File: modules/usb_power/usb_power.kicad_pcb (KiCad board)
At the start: 2 copper layers, 30.5 x 68.6 mm, 11 parts, among them J1 USB_C_Receptacle_PowerOnly_6P

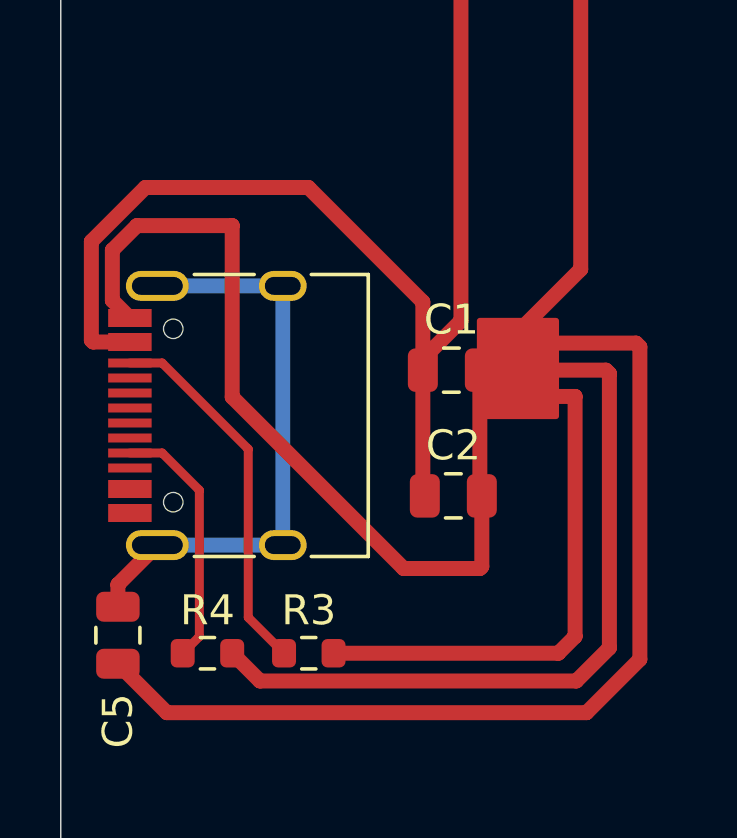
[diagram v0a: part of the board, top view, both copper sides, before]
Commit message: Changed the orientation of the USB C port
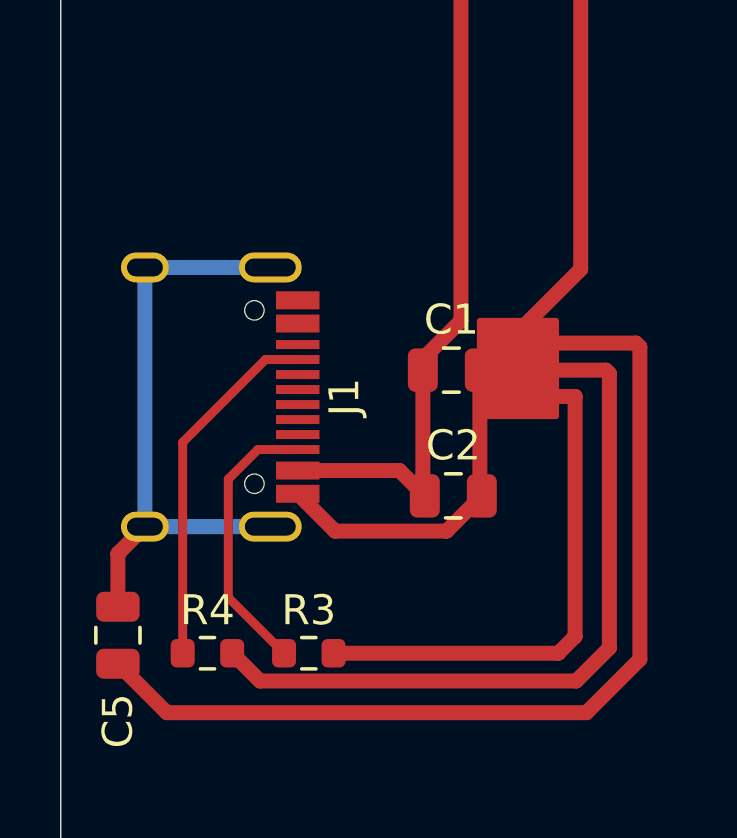
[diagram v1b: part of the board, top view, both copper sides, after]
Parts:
- J1: footprint Connector_USB:USB_C_Receptacle_HRO_TYPE-C-31-M-12 -> BreadModular_TypeC:HRO-TYPE-C-31-M-12
- moved J1 6.18 mm to (47.2, 74.9), turned to -90 degrees
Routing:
- net GND: track 197.5 -> 179.0 mm
- net Net-(C1-Pad1): track 39.0 -> 23.3 mm
- net Net-(J1-CC1): track 8.49 -> 12.0 mm
- net Net-(J1-CC2): track 12.4 -> 9.30 mm

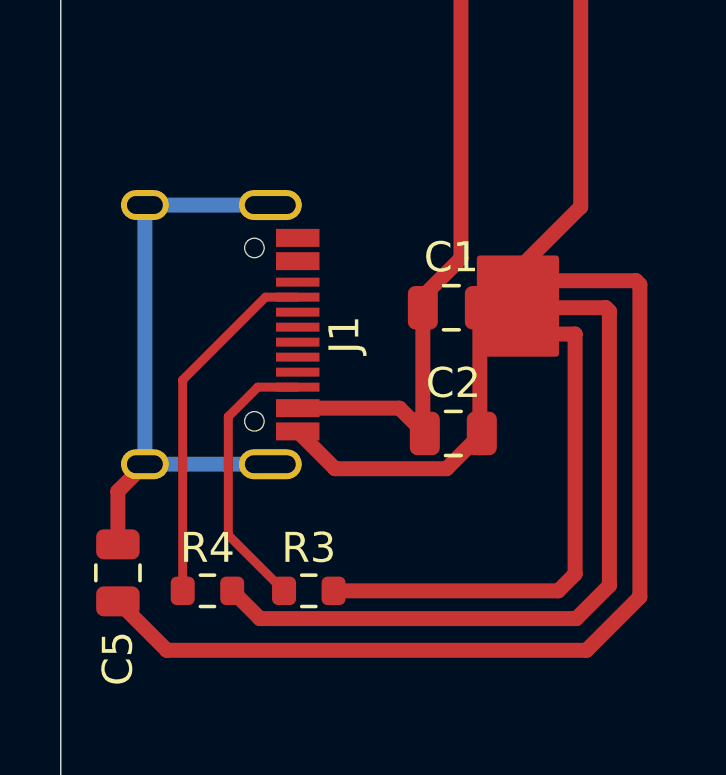
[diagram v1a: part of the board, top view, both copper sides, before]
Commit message: Change usb_power for the TypeC footprint update.
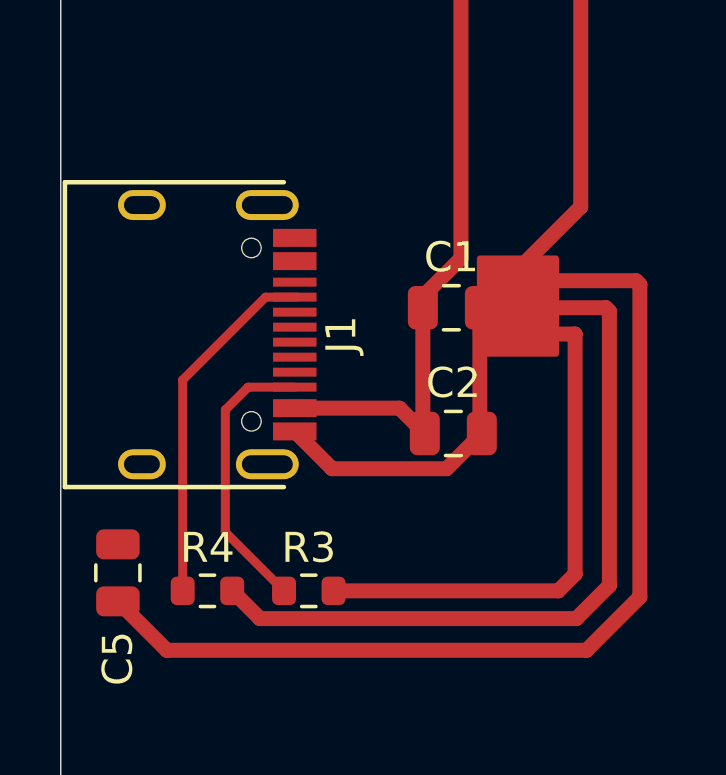
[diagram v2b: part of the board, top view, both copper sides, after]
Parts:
- moved J1 0.10 mm to (47.1, 74.9)
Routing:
- net Net-(J1-SHIELD): track 20.0 -> 0.00 mm

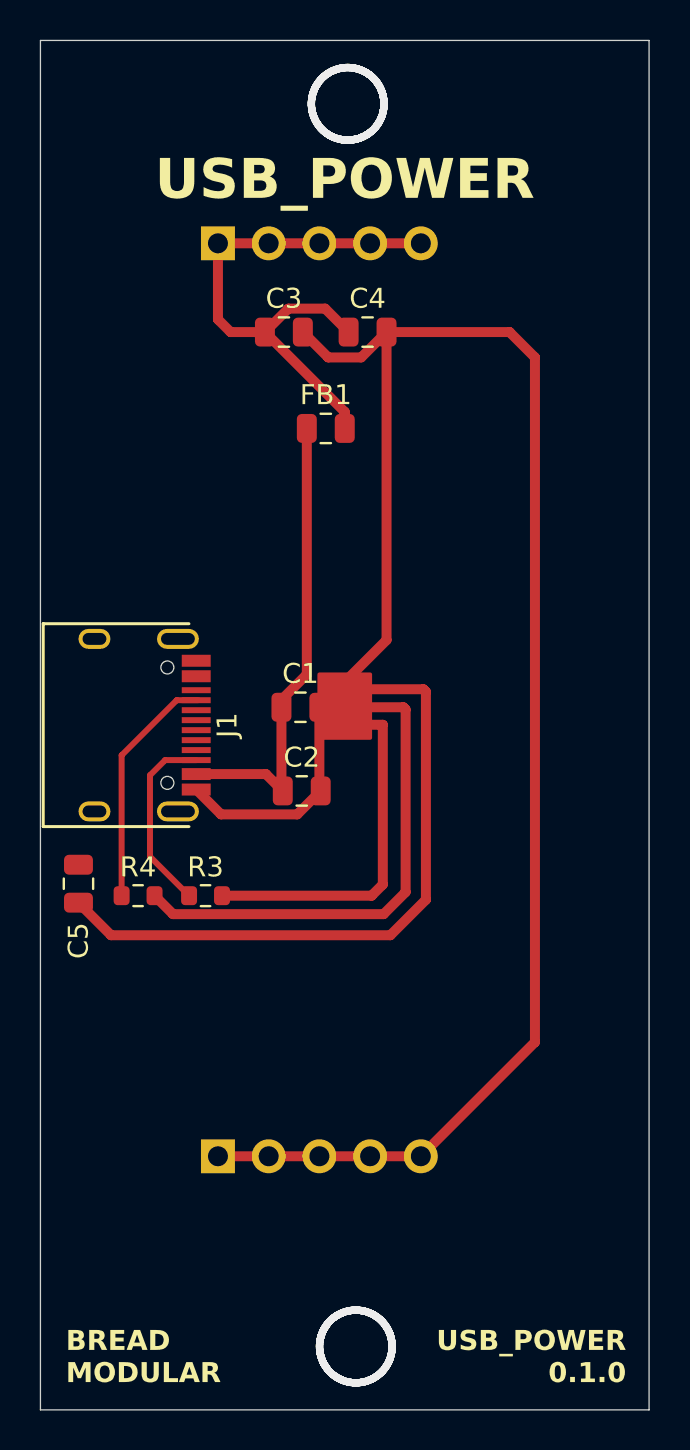
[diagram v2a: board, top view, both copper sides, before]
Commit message: Update usb_power to regulate as 3.3V
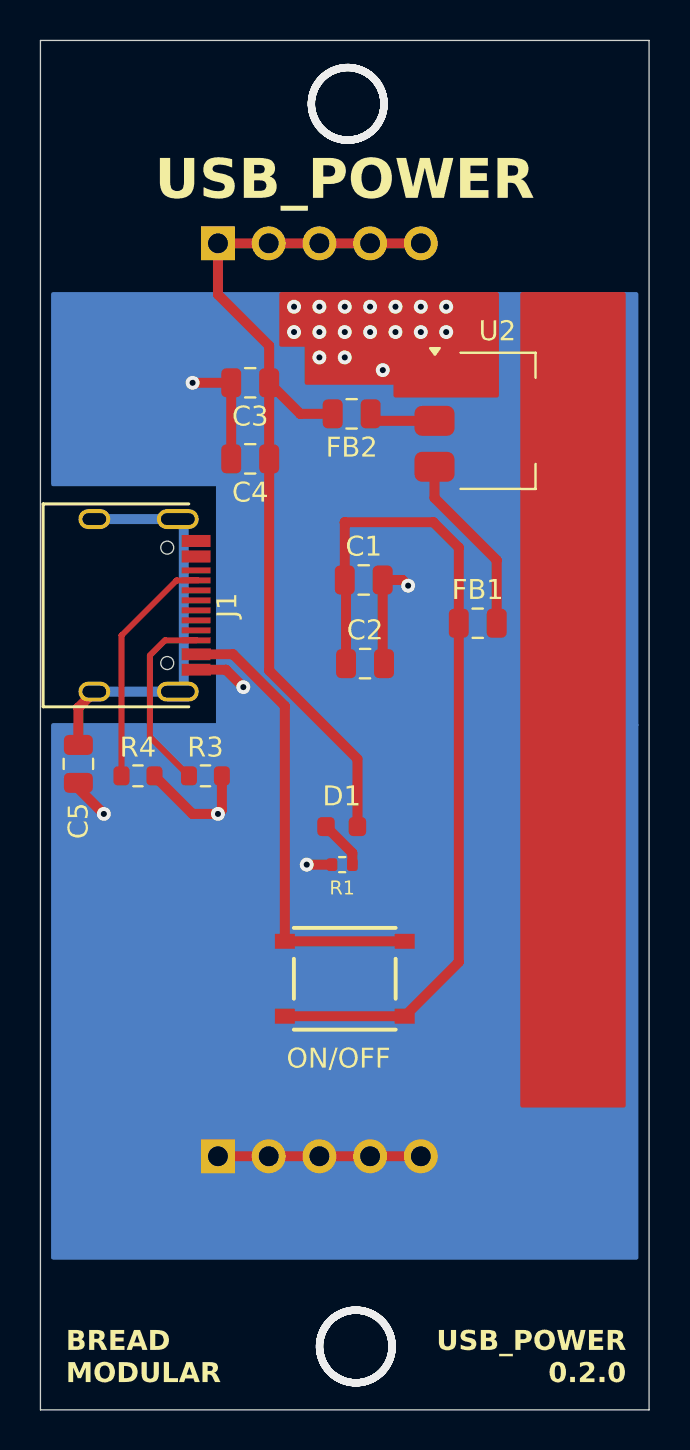
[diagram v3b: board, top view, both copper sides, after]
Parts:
- added D1: LED, LED_SMD:LED_0603_1608Metric, F.Cu at (62.1, 80.0)
- added FB2: GZ2012E800TF, Capacitor_SMD:C_0805_2012Metric, F.Cu at (62.6, 59.3)
- added R1: 1k, Resistor_SMD:R_0402_1005Metric, F.Cu at (62.1, 81.9)
- added SW1: SW_SPST, BreadModular_MISC:SPST_TS-1187A-B-A-B, F.Cu at (62.2, 87.6)
- added U2: AMS1117-3.3, Package_TO_SOT_SMD:SOT-223, F.Cu at (69.9, 59.7)
- moved FB1 12.4 mm to (68.9, 69.8)
- moved C4 8.65 mm to (57.5, 61.6), turned to 180 degrees
- moved C1 7.12 mm to (63.2, 67.7)
- moved C2 7.12 mm to (63.2, 71.9)
- moved C5 6.00 mm to (48.9, 76.9)
- moved J1 6.00 mm to (47.1, 68.9)
- moved R3 6.00 mm to (55.3, 77.5)
- moved R4 6.00 mm to (51.9, 77.5)
- moved C3 3.05 mm to (57.5, 57.8), turned to 180 degrees
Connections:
- 5V1 pad 1: +5V -> +3.3V
- 5V1 pad 2: +5V -> +3.3V
- 5V1 pad 3: +5V -> +3.3V
- 5V1 pad 4: +5V -> +3.3V
- 5V1 pad 5: +5V -> +3.3V
- C1 pad 1: Net-(C1-Pad1) -> Net-(SW1-B)
- C2 pad 1: Net-(C1-Pad1) -> Net-(SW1-B)
- C3 pad 1: +5V -> +3.3V
- C4 pad 1: +5V -> +3.3V
- FB1 pad 1: Net-(C1-Pad1) -> Net-(SW1-B)
- FB1 pad 2: +5V -> Net-(U2-VI)
- J1 pad A9: Net-(C1-Pad1) -> Net-(SW1-A)
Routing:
- net GND: track 179.1 -> 36.2 mm, vias 0 -> 23
- net +3.3V: track 0.00 -> 46.1 mm
- net Net-(SW1-B): track 0.00 -> 43.9 mm
- net +5V: track 28.2 -> 0.00 mm
- net Net-(SW1-A): track 0.00 -> 23.3 mm
- net Net-(C1-Pad1): track 23.3 -> 0.00 mm
- net Net-(J1-SHIELD): track 0.00 -> 20.2 mm
- net Net-(U2-VI): track 0.00 -> 9.13 mm
- net Net-(U2-VO): track 0.00 -> 3.34 mm
- net Net-(D1-K): track 0.00 -> 2.45 mm
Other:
- board text added: "ON/OFF"
- board text added: "USB_POWER 0.2.0"
- board text removed: "USB_POWER 0.1.0"

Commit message: Removed the usb_power tactile switch
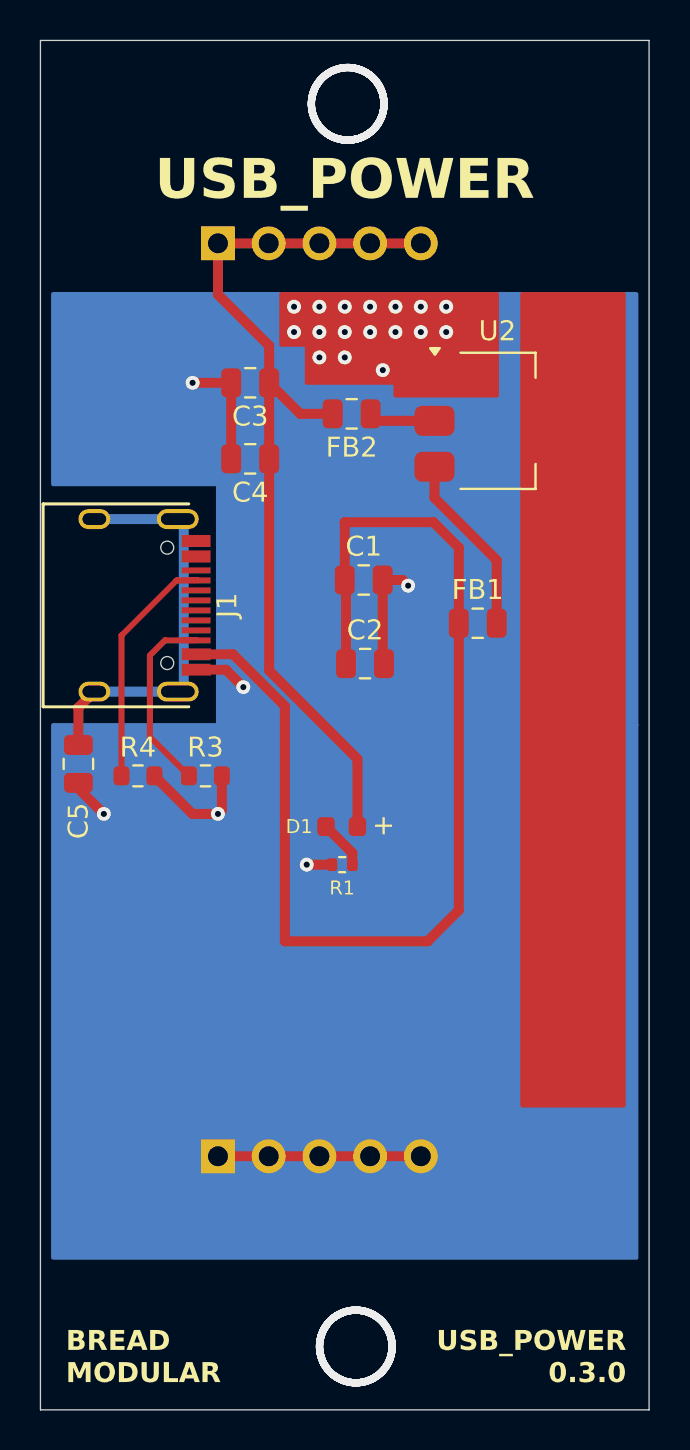
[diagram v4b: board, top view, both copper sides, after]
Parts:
- removed SW1: SW_SPST, BreadModular_MISC:SPST_TS-1187A-B-A-B
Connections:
- C1 pad 1: Net-(SW1-B) -> Net-(C1-Pad1)
- C2 pad 1: Net-(SW1-B) -> Net-(C1-Pad1)
- FB1 pad 1: Net-(SW1-B) -> Net-(C1-Pad1)
- J1 pad A9: Net-(SW1-A) -> Net-(C1-Pad1)
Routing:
- net Net-(C1-Pad1): track 0.00 -> 58.2 mm
- net Net-(SW1-B): track 43.9 -> 0.00 mm
- net Net-(SW1-A): track 23.3 -> 0.00 mm
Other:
- board text added: "USB_POWER 0.3.0"
- board text removed: "ON/OFF"
- board text removed: "USB_POWER 0.2.0"
